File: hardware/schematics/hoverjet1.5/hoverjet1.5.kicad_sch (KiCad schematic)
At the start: 1 part, among them J9 Conn_02x20_Odd_Even

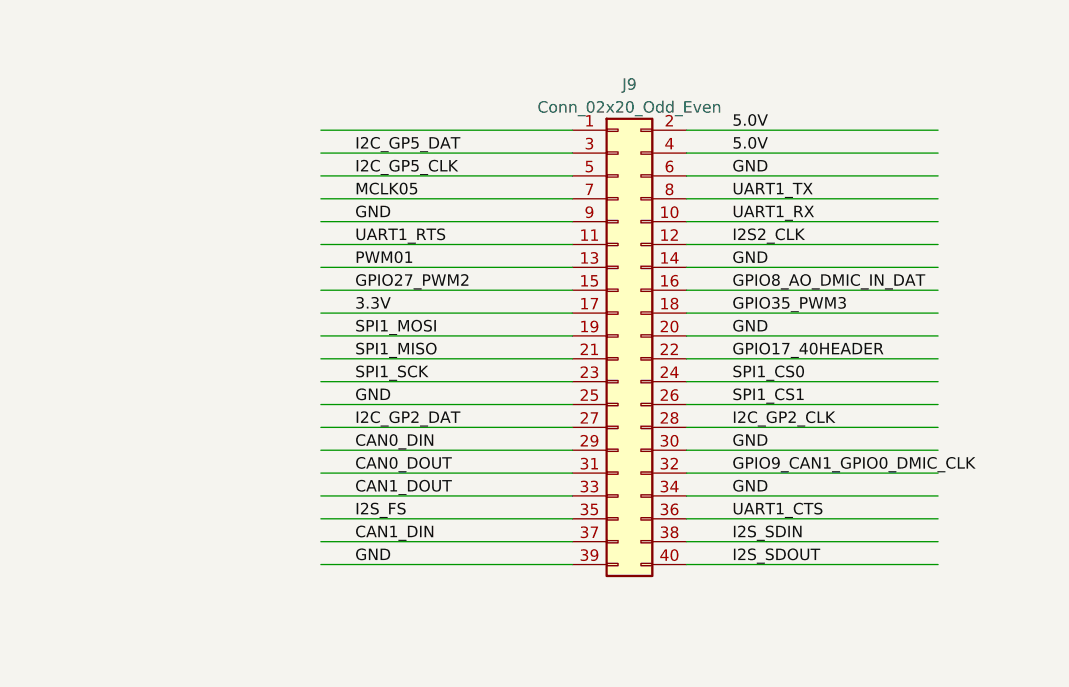
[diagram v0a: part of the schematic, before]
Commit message: added adafruit current sense breakout
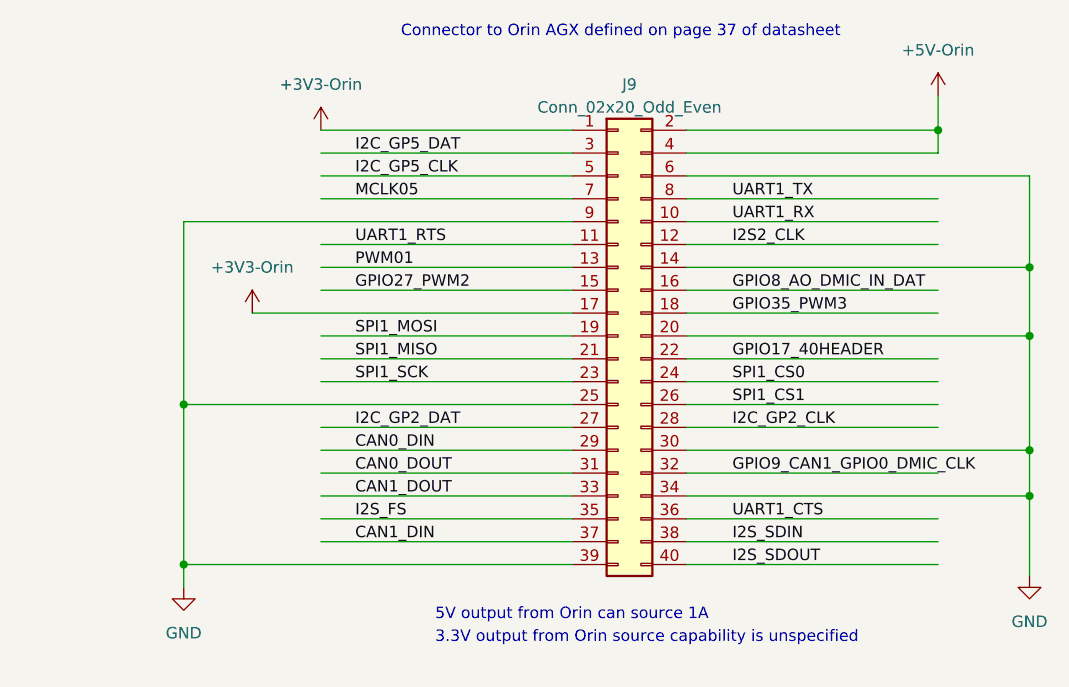
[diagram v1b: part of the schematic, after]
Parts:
- J9: footprint (none) -> Connector_PinHeader_2.54mm:PinHeader_2x20_P2.54mm_Horizontal
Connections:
- net 3.3V is gone; now on net +3V3-Orin: J9.17 (Pin_17)
- net +3V3-Orin: now reaches J9.1 (Pin_1)
- net 5.0V renamed +5V-Orin
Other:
- note added: "3.3V output from Orin source capability is unspecified"
- note added: "5V output from Orin can source 1A"
- note added: "Connector to Orin AGX defined on page 37 of datasheet"

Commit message: syncing hardware changes
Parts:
- added M5: 1083, symbol hoverjet:1083
- added R2 (x5): 10k, Resistor_SMD:R_0603_1608Metric_Pad0.98x0.95mm_HandSolder, symbol Device:R
- added R2 (x3): 56.2k, Resistor_SMD:R_0603_1608Metric_Pad0.98x0.95mm_HandSolder, symbol Device:R
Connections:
- net +3V3-Orin: now also M5.1 (VCC)
- net +5V-Orin: now also R2.1
- net GND: now also M5.11 (GND), M5.12 (GND), R2.2, R2.2, R2.2, R2.2
- new net: M5.8 (AIN1), R2.1, R2.2
- new net: M5.7 (AIN0), R2.1, R2.2
- new net: M5.9 (AIN2), R2.1, R2.2
- new net: M5.10 (AIN3), R2.1, R2.2
- new net +15V: R2.1
- new net +BATT: R2.1
- new net SCL: M5.3 (SCL)
- new net SDA: M5.4 (SDA)
- new net VBUS: R2.1
- no-connect marks 0 -> 3
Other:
- added sheet Pose (pose.kicad_sch)
